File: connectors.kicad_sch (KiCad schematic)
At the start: 6 parts, among them J1 Conn_02x05_Odd_Even, J2 USB_C_Receptacle_USB2.0, J3 Conn_02x05_Odd_Even, J4 Conn_02x05_Odd_Even

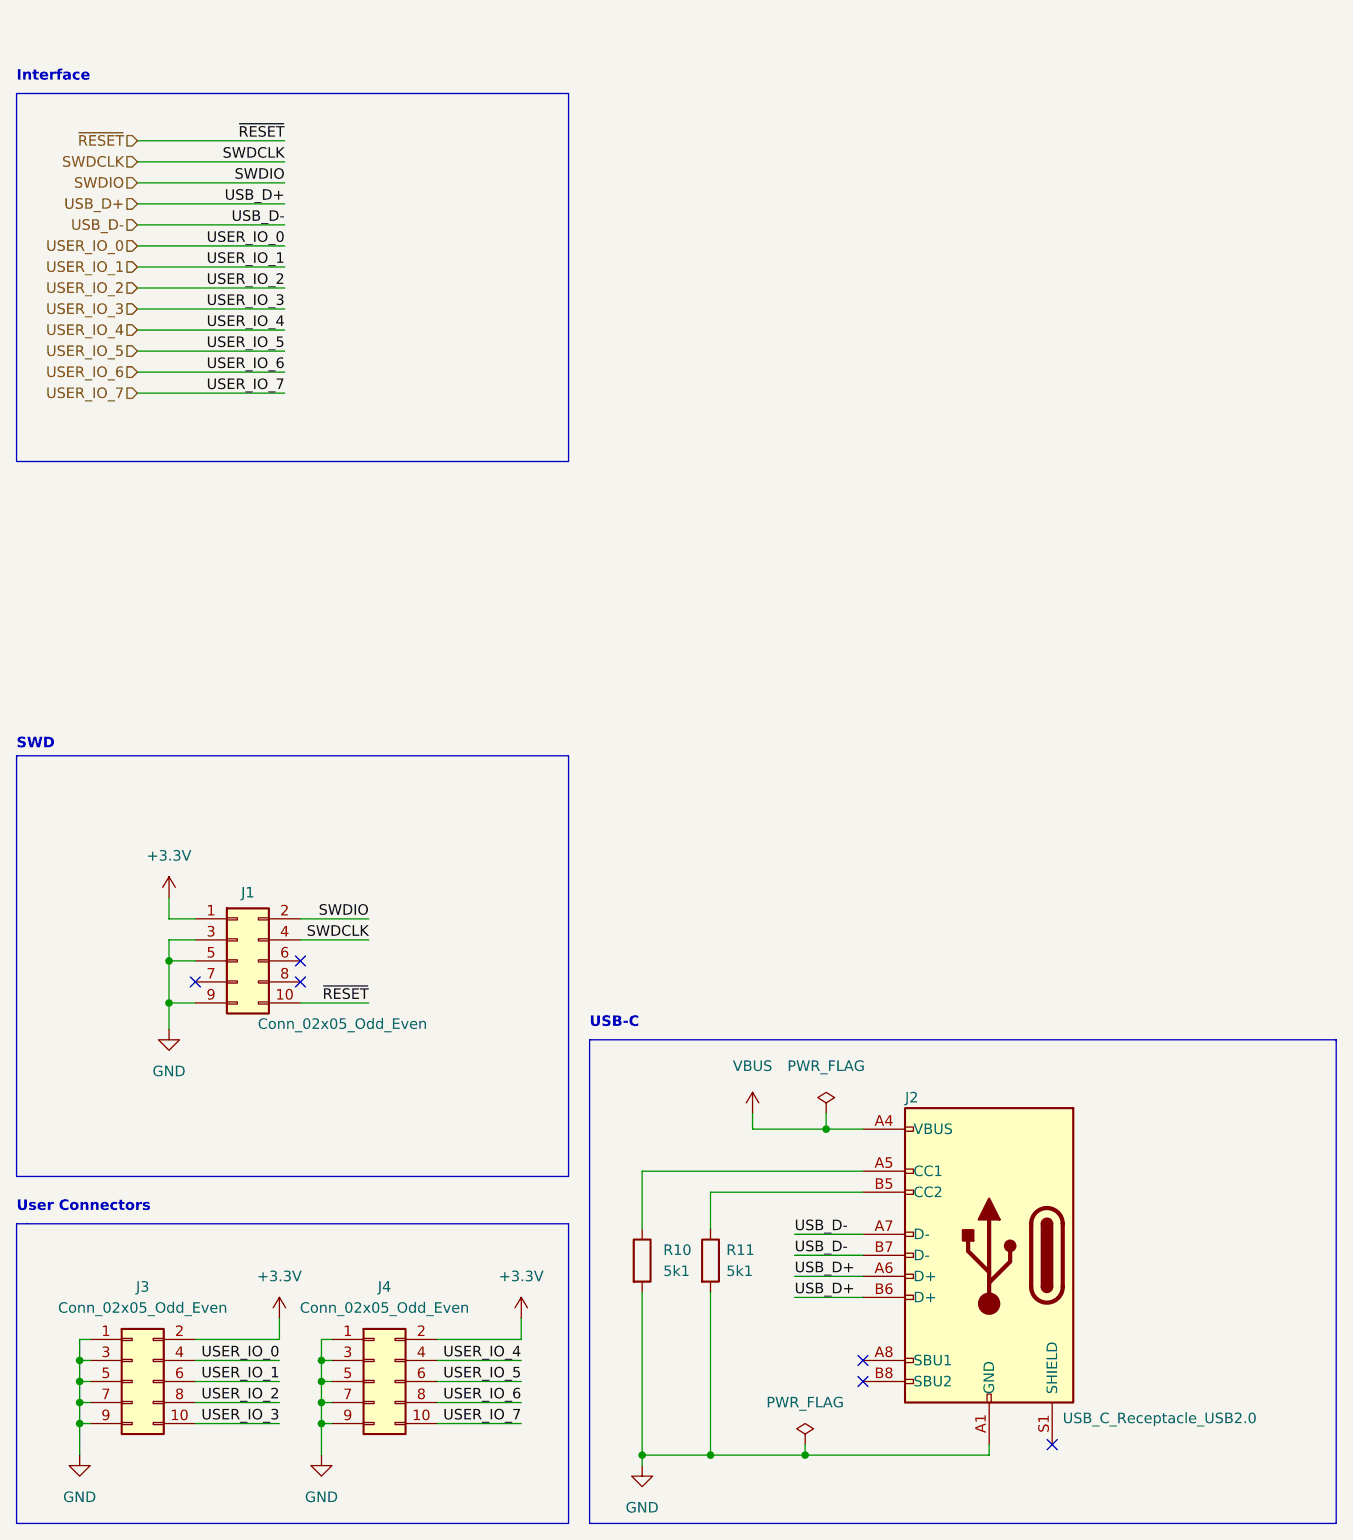
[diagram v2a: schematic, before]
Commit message: Basic routing MCU, crystal, flash, crypto
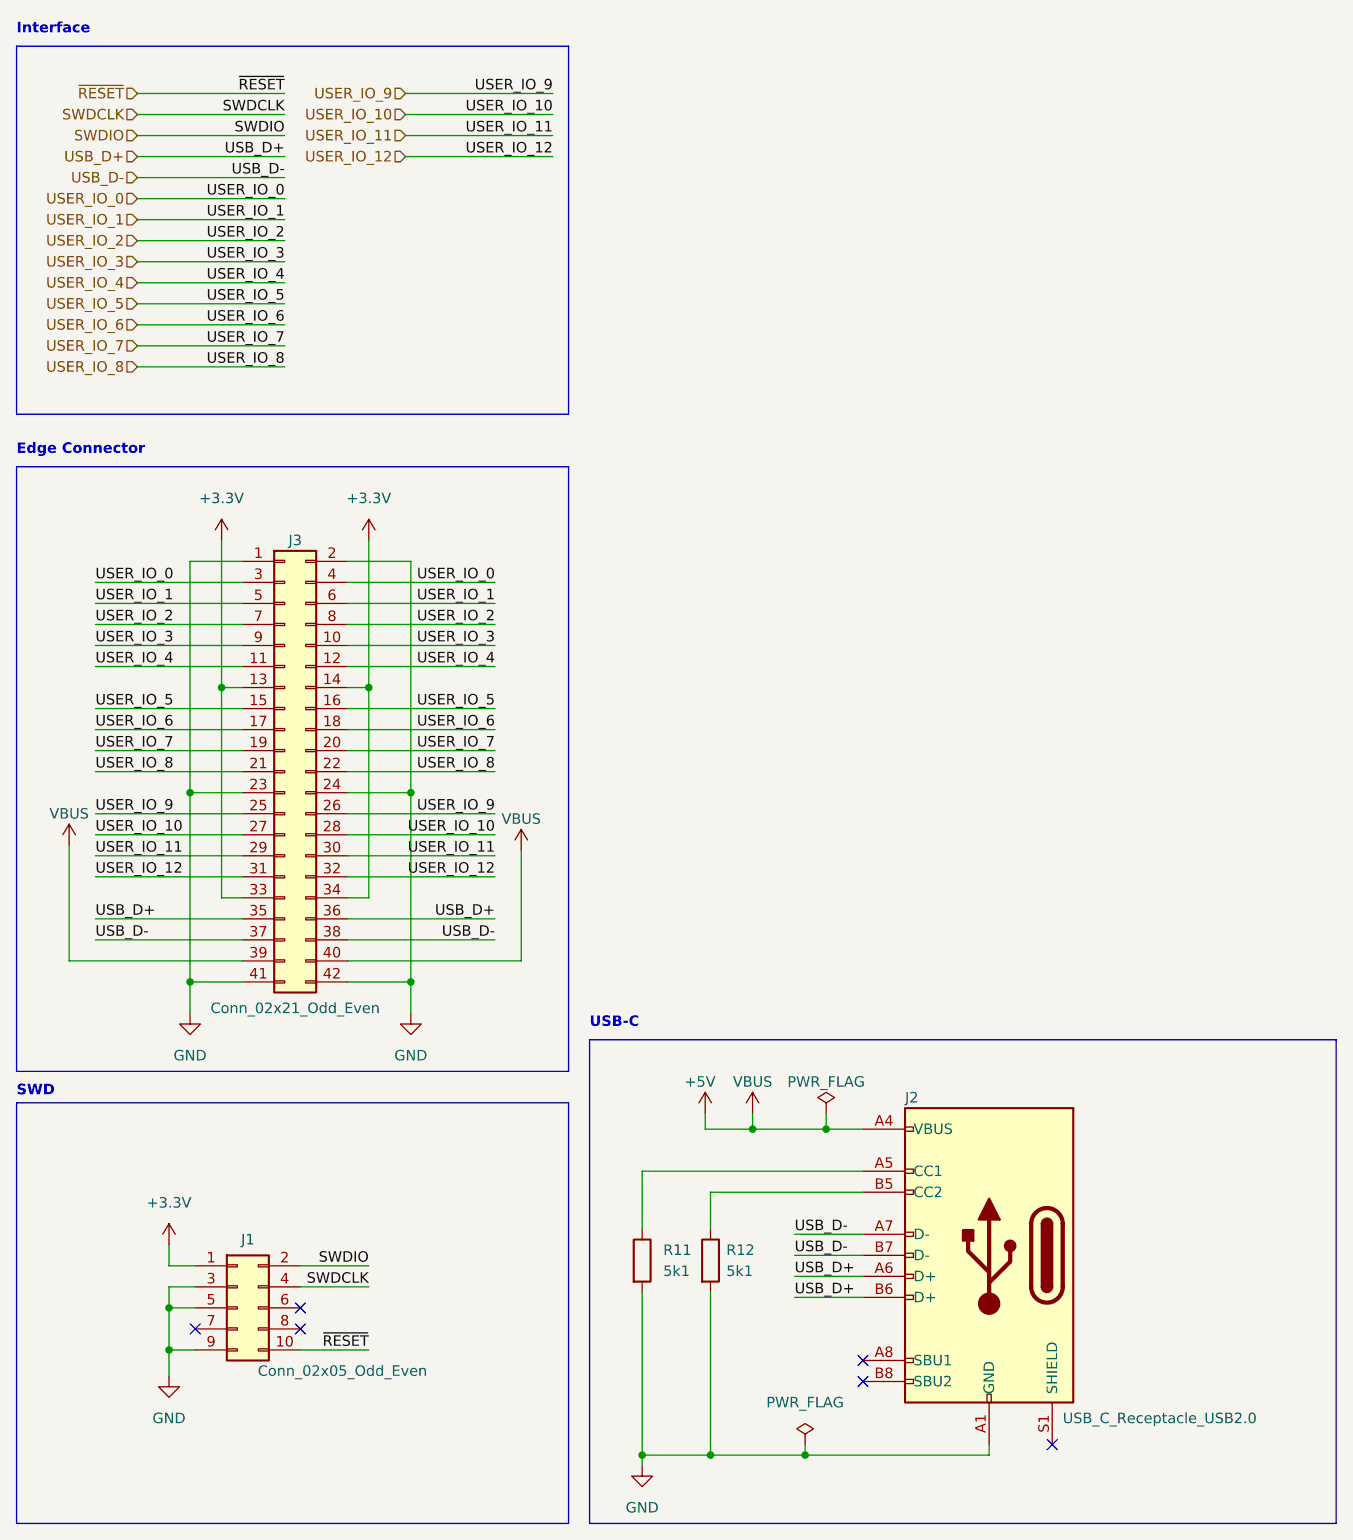
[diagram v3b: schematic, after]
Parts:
- removed J3, J4: Conn_02x05_Odd_Even, Connector_Hirose:Hirose_DF12_DF12C3.0-10DS-0.5V_2x05_P0.50mm_Vertical, symbol Connector_Generic:Conn_02x05_Odd_Even
- added J3: Conn_02x21_Odd_Even, pico-card:PICO_CARD_EDGE_21, symbol Connector_Generic:Conn_02x21_Odd_Even
- J1: footprint Connector:Tag-Connect_TC2050-IDC-FP_2x05_P1.27mm_Vertical -> Connector:Tag-Connect_TC2050-IDC-NL_2x05_P1.27mm_Vertical
- renumbered R10 to R11, R11 to R12
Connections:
- net +3V3: now also J3.13 (Pin_13), J3.14 (Pin_14), J3.33 (Pin_33), J3.34 (Pin_34)
- net GND: now also J3.1 (Pin_1), J3.2 (Pin_2), J3.23 (Pin_23), J3.24 (Pin_24), J3.41 (Pin_41), J3.42 (Pin_42)
- net USB_D+: now also J3.35 (Pin_35), J3.36 (Pin_36)
- net USB_D-: now also J3.37 (Pin_37), J3.38 (Pin_38)
- net USER_IO_0: now also J3.3 (Pin_3), J3.4 (Pin_4)
- net USER_IO_1: now also J3.5 (Pin_5), J3.6 (Pin_6)
- net USER_IO_2: now also J3.7 (Pin_7), J3.8 (Pin_8)
- net USER_IO_3: now also J3.10 (Pin_10), J3.9 (Pin_9)
- net USER_IO_4: now also J3.11 (Pin_11), J3.12 (Pin_12)
- net USER_IO_5: now also J3.15 (Pin_15), J3.16 (Pin_16)
- net USER_IO_6: now also J3.17 (Pin_17), J3.18 (Pin_18)
- net USER_IO_7: now also J3.19 (Pin_19), J3.20 (Pin_20)
- net VBUS renamed +5V
- net +5V: now also J3.39 (Pin_39), J3.40 (Pin_40)
- new net USER_IO_10: J3.27 (Pin_27), J3.28 (Pin_28)
- new net USER_IO_11: J3.29 (Pin_29), J3.30 (Pin_30)
- new net USER_IO_12: J3.31 (Pin_31), J3.32 (Pin_32)
- new net USER_IO_8: J3.21 (Pin_21), J3.22 (Pin_22)
- new net USER_IO_9: J3.25 (Pin_25), J3.26 (Pin_26)
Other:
- note added: "Edge Connector"
- note removed: "User Connectors"
- moved on the sheet: J1

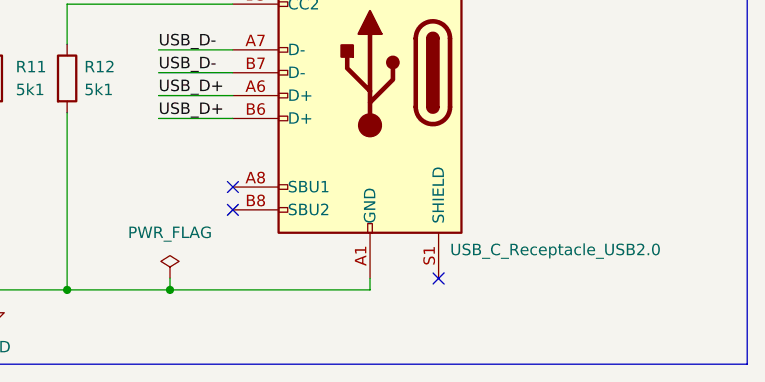
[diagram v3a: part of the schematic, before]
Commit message: Basic routing complete, rename
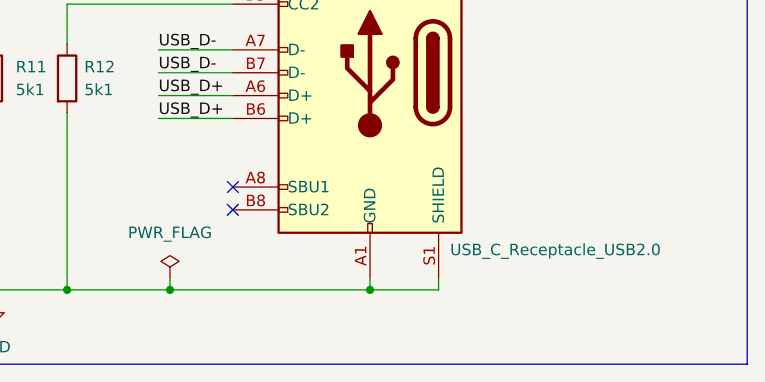
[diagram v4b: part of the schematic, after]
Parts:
- J3: footprint pico-card:PICO_CARD_EDGE_21 -> Diva-Card:PICO_CARD_EDGE_21
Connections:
- net GND: now also J2.S1 (SHIELD)
- no-connect marks 6 -> 5
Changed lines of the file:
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@@
   (junction (at 33.02 173.99) (diameter 0) (color 0 0 0 0)
+  )
+  (junction (at 132.08 186.69) (diameter 0) (color 0 0 0 0)
   )
   (no_connect (at 36.195 171.45))
@@
   (no_connect (at 48.895 168.91))
   (no_connect (at 116.84 177.8))
-  (no_connect (at 139.7 185.42))
   (polyline (pts (xy 14.605 144.145) (xy 81.28 144.145))
     (stroke (width 0) (type default) (color 0 0 0 0))
@@
     (stroke (width 0) (type default) (color 0 0 0 0))
   )
+  (wire (pts (xy 139.7 185.42) (xy 139.7 186.69))
+    (stroke (width 0) (type default) (color 0 0 0 0))
+  )
   (wire (pts (xy 29.21 27.305) (xy 46.99 27.305))
     (stroke (width 0) (type default) (color 0 0 0 0))
@@
   )
   (wire (pts (xy 54.61 127) (xy 75.565 127))
+    (stroke (width 0) (type default) (color 0 0 0 0))
+  )
+  (wire (pts (xy 139.7 186.69) (xy 132.08 186.69))
     (stroke (width 0) (type default) (color 0 0 0 0))
   )
@@
     (property "Reference" "J3" (id 0) (at 48.26 76.2 0))
     (property "Value" "Conn_02x21_Odd_Even" (id 1) (at 48.26 132.715 0))
-    (property "Footprint" "pico-card:PICO_CARD_EDGE_21" (id 2) (at 46.99 104.14 0)
-      (effects (font (size 1.27 1.27)) hide)
-    )
+    (property "Footprint" "Diva-Card:PICO_CARD_EDGE_21" (id 2) (at 46.99 104.14 0)
+      (effects (font (size 1.27 1.27)) hide)
+    )

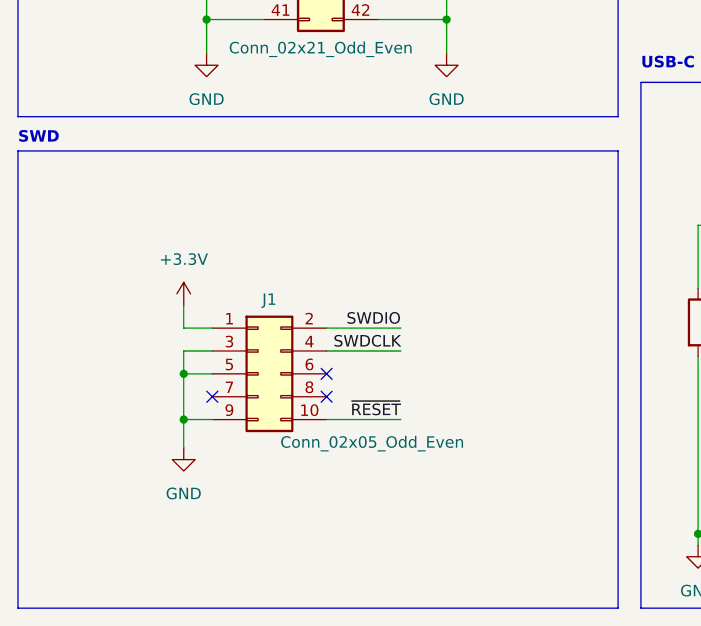
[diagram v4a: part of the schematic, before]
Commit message: updating footprints to udfn
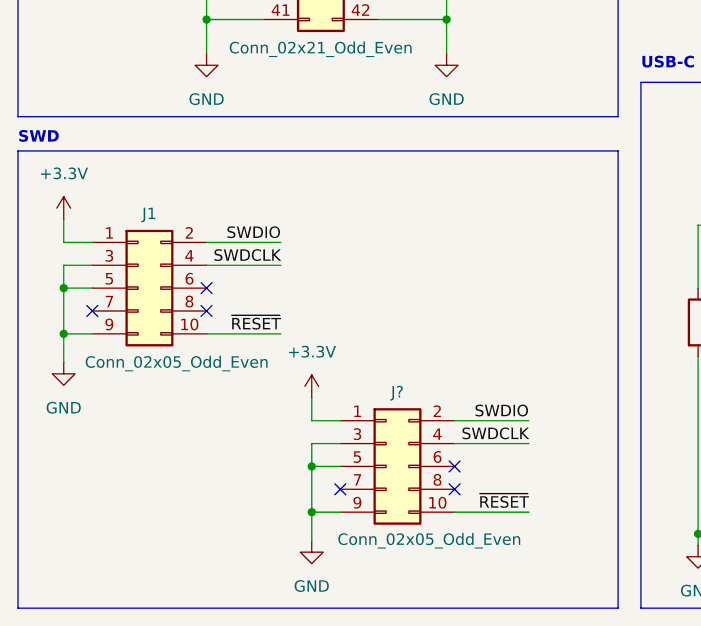
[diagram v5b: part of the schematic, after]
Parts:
- added J?: Conn_02x05_Odd_Even, Connector:Tag-Connect_TC2050-IDC-NL_2x05_P1.27mm_Vertical, symbol Connector_Generic:Conn_02x05_Odd_Even
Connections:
- net +3V3: now also J?.1 (Pin_1)
- net GND: now also J?.3 (Pin_3), J?.5 (Pin_5), J?.9 (Pin_9)
- net SWDCLK: now also J?.4 (Pin_4)
- net SWDIO: now also J?.2 (Pin_2)
- net ~{RESET}: now also J?.10 (Pin_10)
- no-connect marks 5 -> 8
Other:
- moved on the sheet: J1

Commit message: Adding schematic pdf
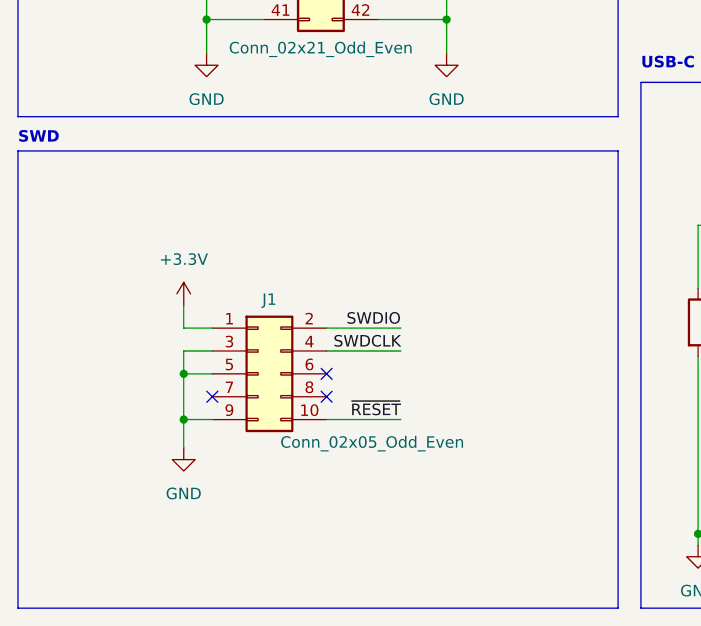
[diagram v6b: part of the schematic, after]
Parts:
- removed J?: Conn_02x05_Odd_Even, Connector:Tag-Connect_TC2050-IDC-NL_2x05_P1.27mm_Vertical, symbol Connector_Generic:Conn_02x05_Odd_Even
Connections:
- no-connect marks 8 -> 5
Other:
- company: (none) -> DIVA ENG
- title: (none) -> Pico Card
- moved on the sheet: J1
